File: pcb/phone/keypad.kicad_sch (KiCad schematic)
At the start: 29 parts, among them SW1 SKQGABE010, SW10 SKQGABE010, SW11 SKQGABE010, SW12 SKQGABE010, SW13 SKQGABE010, SW14 SKQGABE010, SW15 SKQGABE010, SW16 SKQGABE010, SW17 SKQGABE010, SW18 SKQGABE010, SW19 SKQGABE010, SW2 SKQGABE010, SW20 SKQGABE010, SW3 SKQGABE010, SW4 SKQGABE010, SW5 SKQGABE010, SW6 SKQGABE010, SW7 SKQGABE010, SW8 SKQGABE010, SW9 SKQGABE010

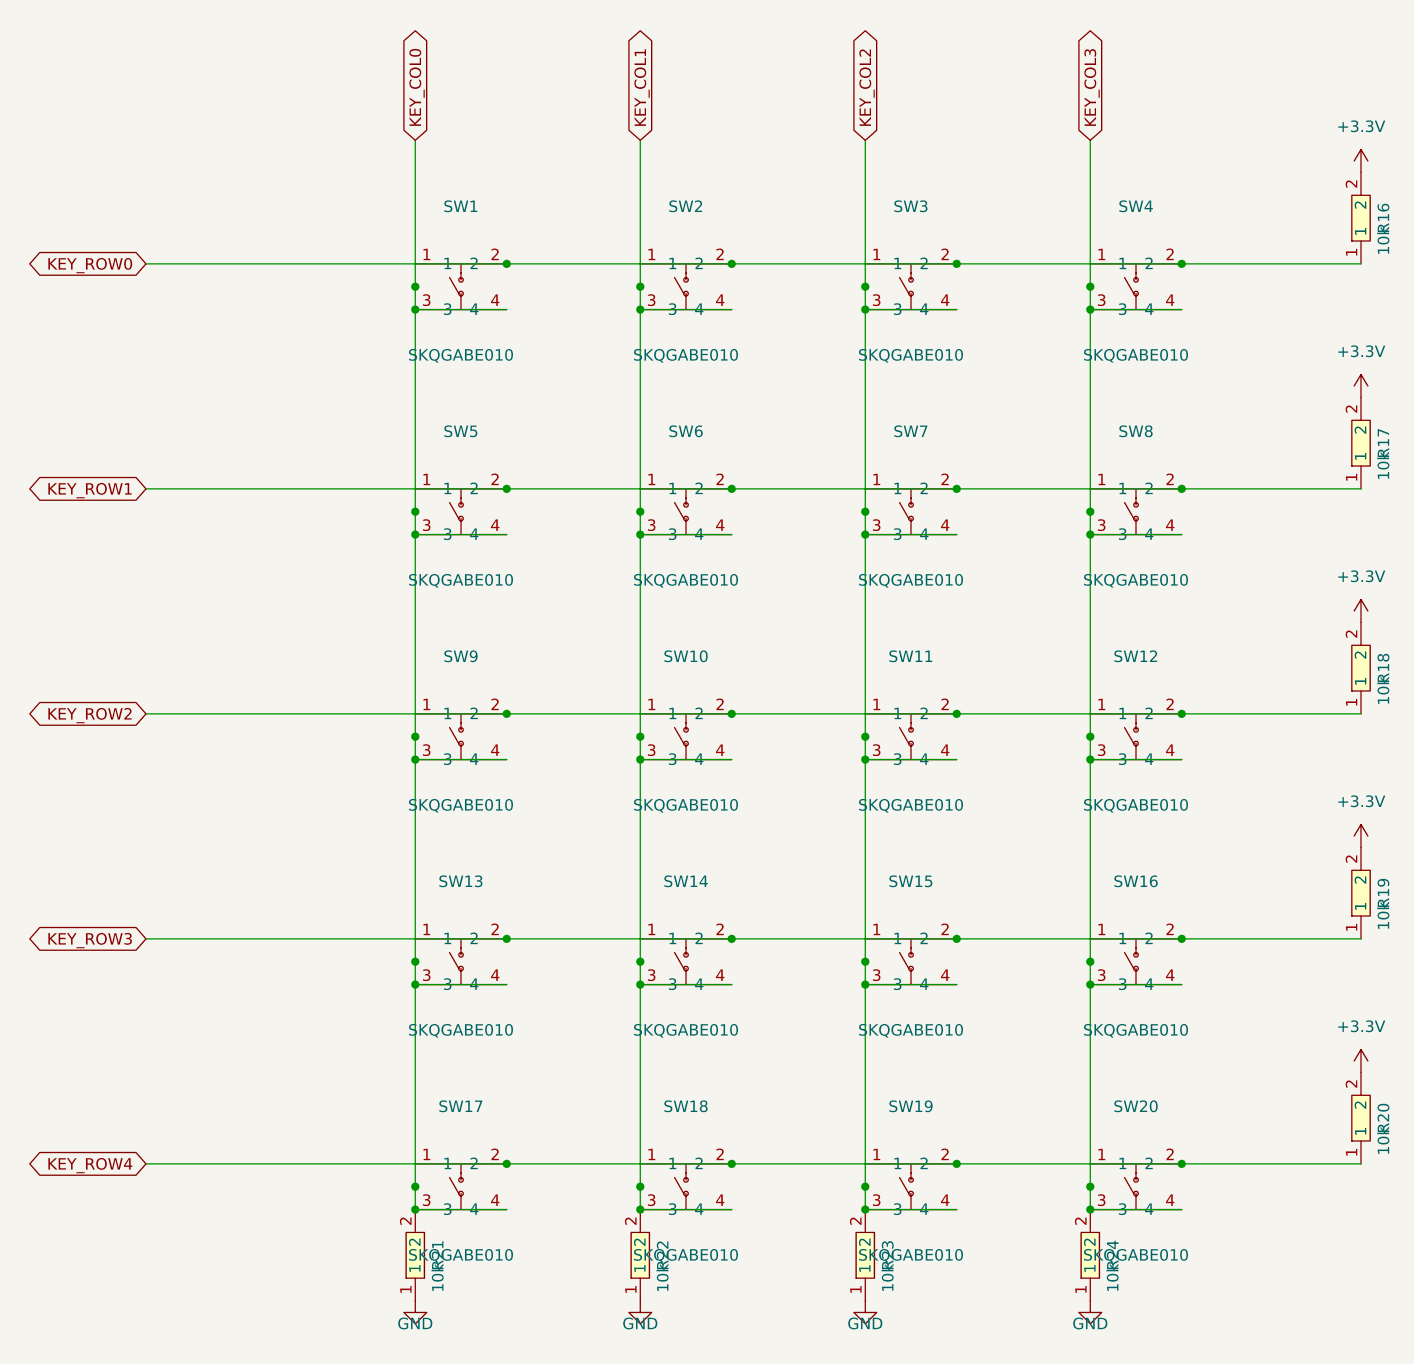
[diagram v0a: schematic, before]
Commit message: Fix keypad schematic: on-grid placement, correct matrix wiring, NC flags
The keypad sheet had three issues from the subagent generation:
1. All switches/wires/labels at 5mm spacing (off 1.27mm grid) causing
   endpoint_off_grid warnings and pin_not_connected errors
2. Column wires connected to Pin1 X instead of Pin2 X, shorting rows
   to columns at every switch
3. Row wires ran at Pin1 Y, passing through Pin2 positions

Fix applied via fix_keypad_full.py:
- Snapped all coordinates to 1.27mm grid (25.4mm switch spacing)
- Row wires now run at SW_Y (switch center) with short vertical wires
  from Pin1 down to the row wire, avoiding Pin2 crossings
- Row wires broken into segments between adjacent Pin1 X positions
  so all wire endpoints connect properly (not mid-wire)
- Column wires at Pin2 X (right side), connecting Pin2 of all switches
- Column labels, pull-down resistors, and GND symbols moved to Pin2 X
- Pull-up resistor wires fixed (pin offset is 5.08, not 2.54)
- NC flags added to Pin 3 (all rows) and Pin 4 (rows 0-3) since these
  are internally connected to Pin 1/Pin 2 in the tactile switch
- Numeric coordinate replacement to handle floating point artifacts
  (e.g., 123.64999999999999 in file vs 123.65 from Python str())

Result: Keypad sheet is now ERC-clean (0 errors, 0 warnings).
Total ERC violations dropped from 402 to 287.

Generated with [Devin](https://devin.ai)

Co-Authored-By: Devin <158243242+devin-ai-integration[bot]@users.noreply.github.com>
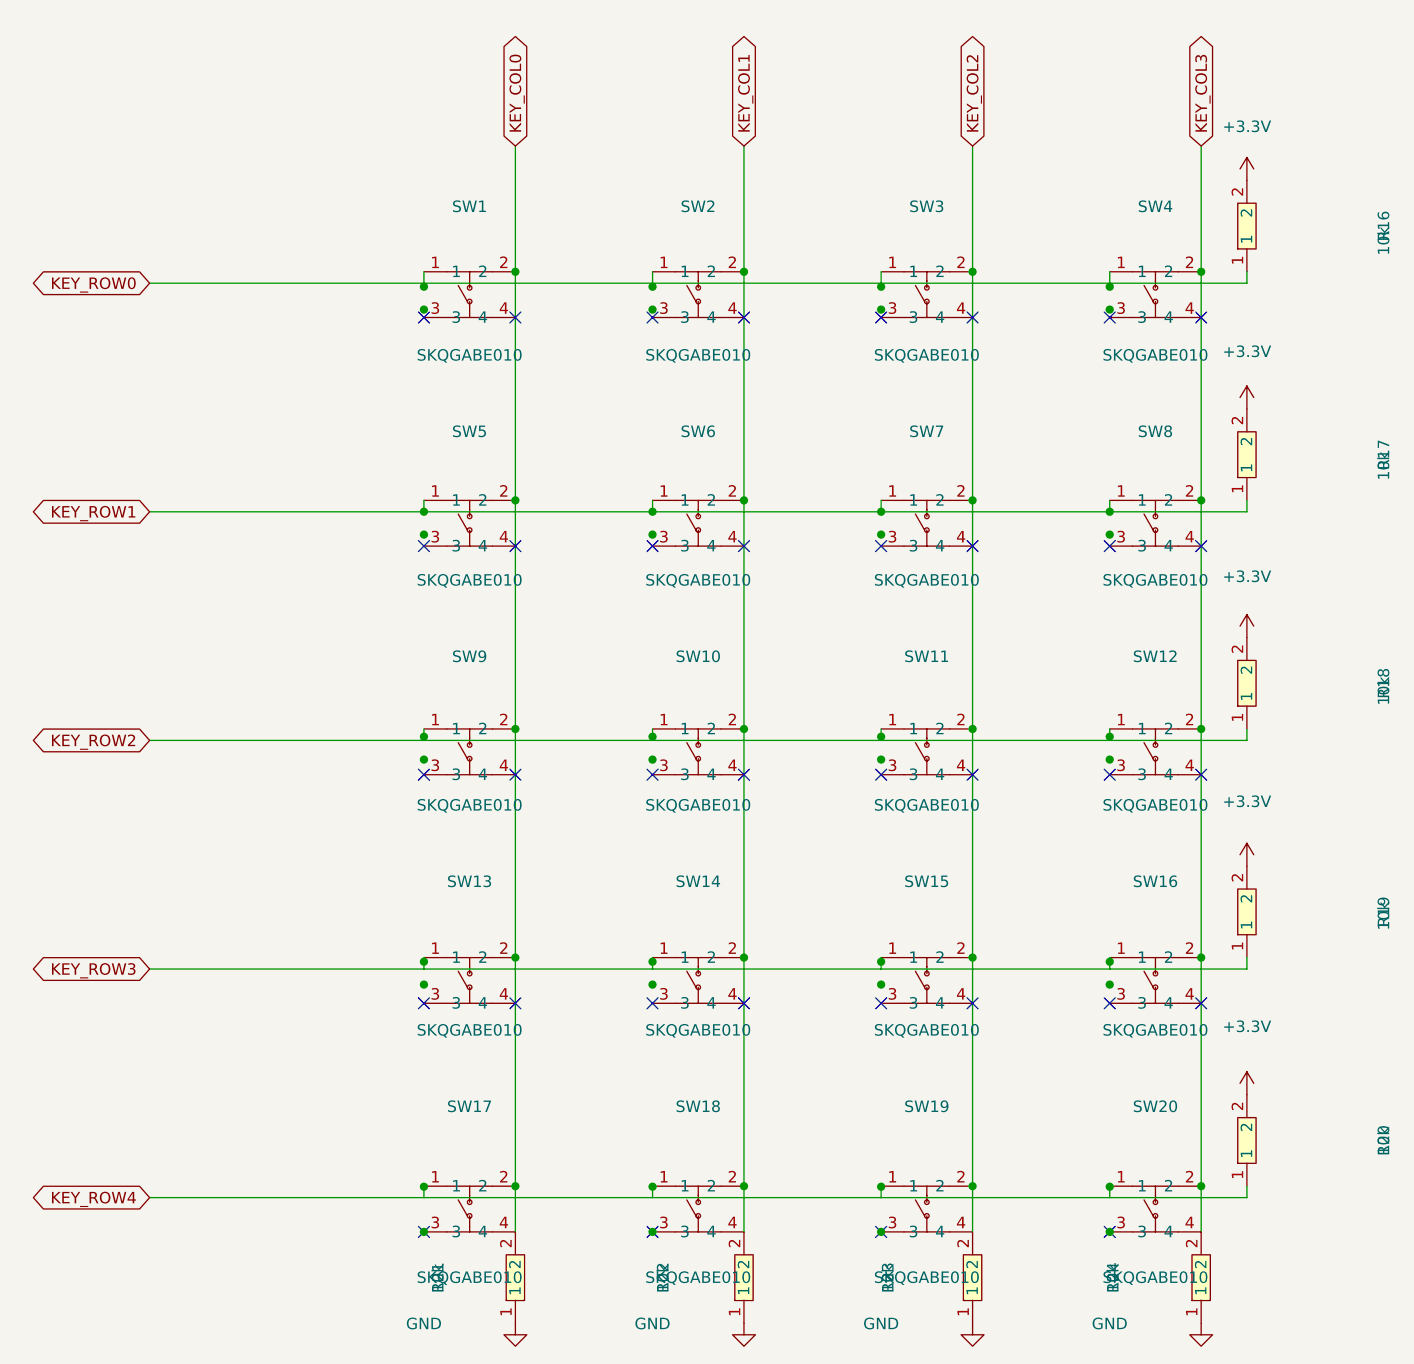
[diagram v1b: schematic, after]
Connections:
- net KEY_COL0: now also SW1.2, SW13.2, SW17.2, SW5.2, SW9.2; no longer SW1.3, SW1.4, SW13.3, SW13.4, SW17.3, SW5.3, SW5.4, SW9.3, SW9.4
- net KEY_COL1: now also SW10.2, SW14.2, SW18.2, SW2.2, SW6.2; no longer SW10.3, SW10.4, SW14.3, SW14.4, SW18.3, SW2.3, SW2.4, SW6.3, SW6.4
- net KEY_COL2: now also SW11.2, SW15.2, SW19.2, SW3.2, SW7.2; no longer SW11.3, SW11.4, SW15.3, SW15.4, SW19.3, SW3.3, SW3.4, SW7.3, SW7.4
- net KEY_COL3: now also SW12.2, SW16.2, SW20.2, SW4.2, SW8.2; no longer SW12.3, SW12.4, SW16.3, SW16.4, SW20.3, SW4.3, SW4.4, SW8.3, SW8.4
- net KEY_ROW0: now also SW1.1, SW2.1, SW3.1, SW4.1; no longer SW1.2, SW2.2, SW3.2, SW4.2
- net KEY_ROW1: now also SW5.1, SW6.1, SW7.1, SW8.1; no longer SW5.2, SW6.2, SW7.2, SW8.2
- net KEY_ROW2: now also SW10.1, SW11.1, SW12.1, SW9.1; no longer SW10.2, SW11.2, SW12.2, SW9.2
- net KEY_ROW3: now also SW13.1, SW14.1, SW15.1, SW16.1; no longer SW13.2, SW14.2, SW15.2, SW16.2
- net KEY_ROW4: now also SW17.1, SW18.1, SW19.1, SW20.1; no longer SW17.2, SW18.2, SW19.2, SW20.2
- no-connect marks 0 -> 36
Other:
- moved on the sheet: R16, R17, R18, R19, R20, R21, R22, R23, R24, SW1, SW10, SW11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
